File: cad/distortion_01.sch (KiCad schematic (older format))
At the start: 83 parts

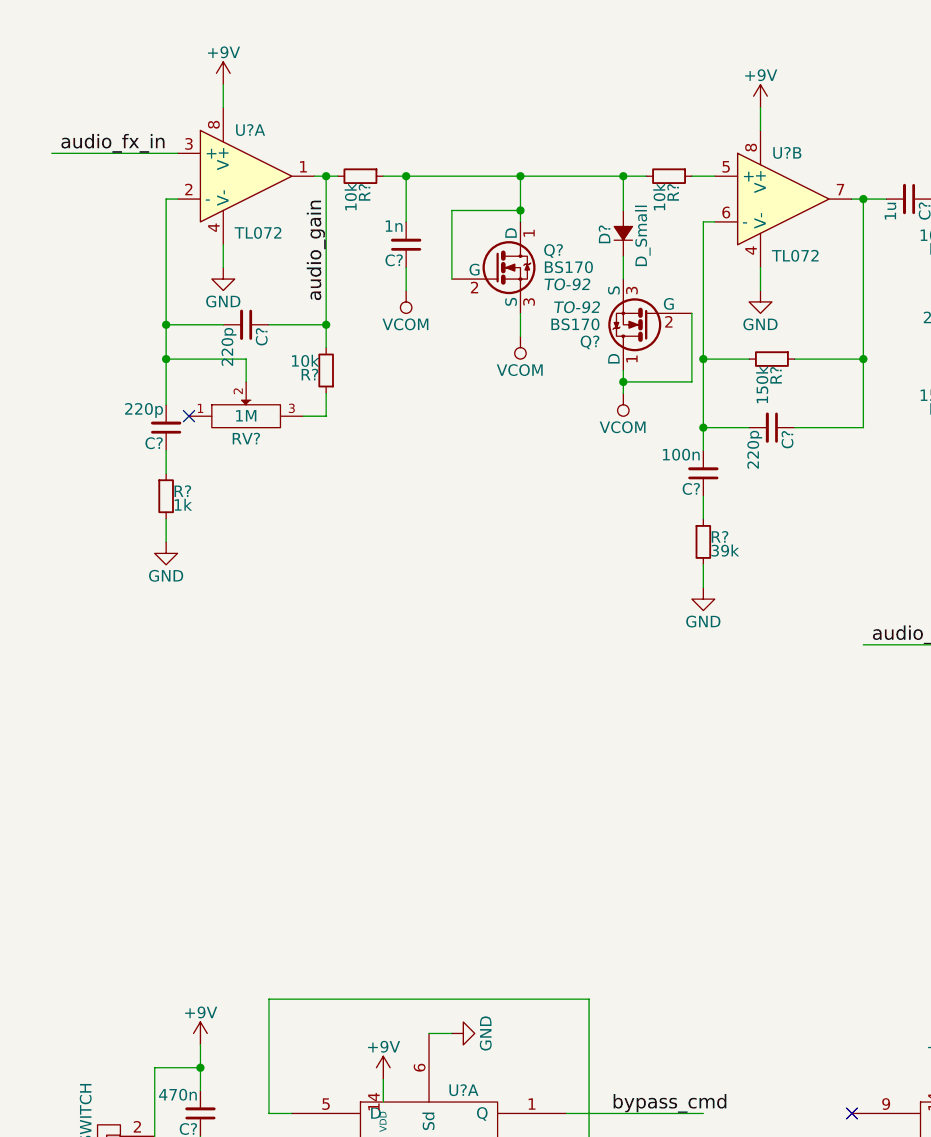
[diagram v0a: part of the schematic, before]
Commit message: Added octave.
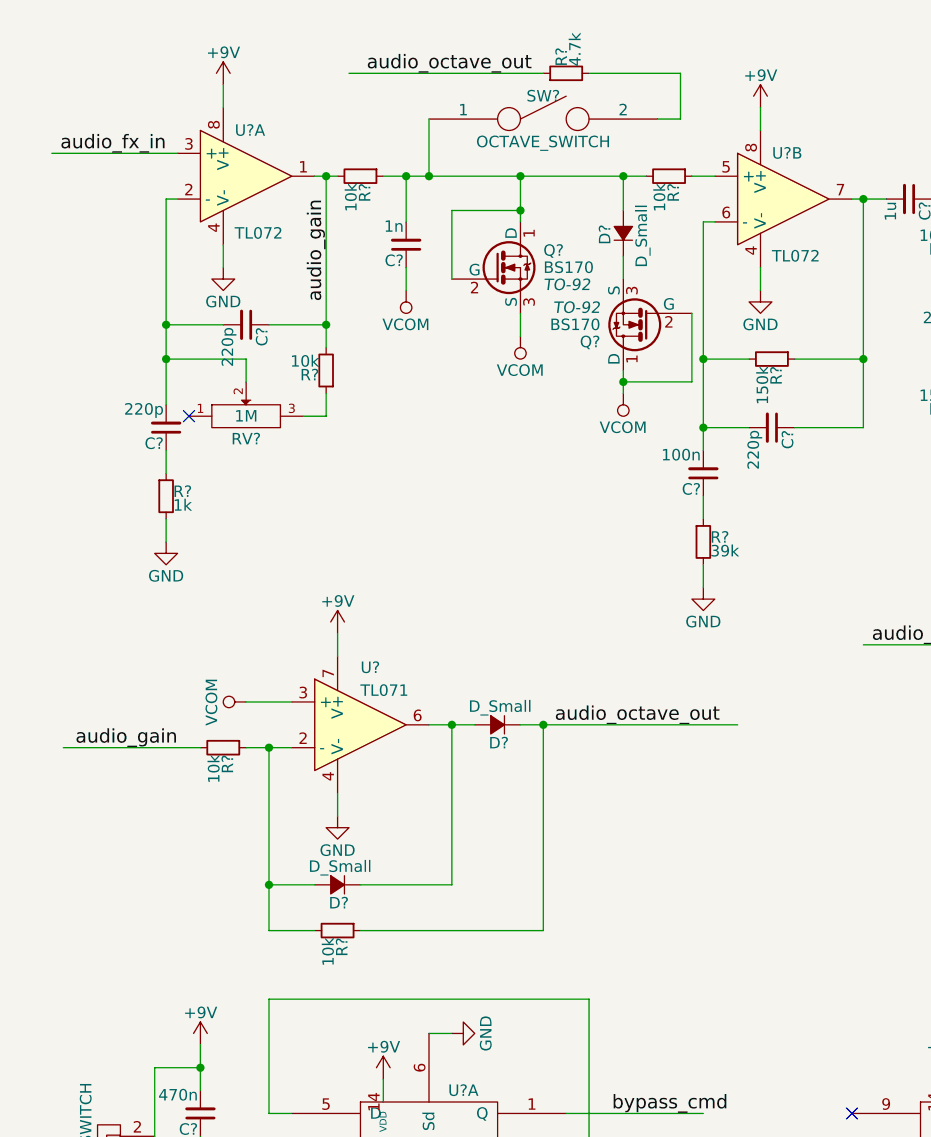
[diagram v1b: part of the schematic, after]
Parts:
- added D? (x2): D_Small, symbol D_Small
- added R? (x2): 10k, symbol R_Small
- added R?: 4.7k, symbol R_Small
- added SW?: OCTAVE_SWITCH, symbol SPST
- added U?: TL071, symbol TL071
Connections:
- net labels added: audio_octave_out
- wire segments 225 -> 244
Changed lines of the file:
@@
 Wire Wire Line
 	4800 3150 4800 3250
+$Comp
+L TL071 U?
+U 1 1 589F853A
+P 2000 3500
+F 0 "U?" H 2000 3750 50  0000 L CNN
+F 1 "TL071" H 2000 3650 50  0000 L CNN
+F 2 "" H 2050 3700 50  0000 C CNN
+F 3 "" H 2000 3750 50  0000 C CNN
+	1    2000 3500
+	1    0    0    -1
+$EndComp
+$Comp
+L +9V #PWR?
+U 1 1 589F8B22
+P 1900 3100
+F 0 "#PWR?" H 1900 2950 50  0001 C CNN
+F 1 "+9V" H 1900 3240 50  0000 C CNN
+F 2 "" H 1900 3100 50  0000 C CNN
+F 3 "" H 1900 3100 50  0000 C CNN
+	1    1900 3100
+	1    0    0    -1
+$EndComp
+$Comp
+L GND #PWR?
+U 1 1 589F8C29
+P 1900 3900
+F 0 "#PWR?" H 1900 3650 50  0001 C CNN
+F 1 "GND" H 1900 3750 50  0000 C CNN
+F 2 "" H 1900 3900 50  0000 C CNN
+F 3 "" H 1900 3900 50  0000 C CNN
+	1    1900 3900
+	1    0    0    -1
+$EndComp
+Wire Wire Line
+	1900 3900 1900 3800
+Wire Wire Line
+	1900 3100 1900 3200
+$Comp
+L D_Small D?
+U 1 1 589F916A
+P 2600 3500
+F 0 "D?" H 2550 3580 50  0000 L CNN
+F 1 "D_Small" H 2450 3420 50  0000 L CNN
+F 2 "" V 2600 3500 50  0000 C CNN
+F 3 "" V 2600 3500 50  0000 C CNN
+	1    2600 3500
+	-1   0    0    1
+$EndComp
+$Comp
+L D_Small D?
+U 1 1 589F92E7
+P 1900 4200
+F 0 "D?" H 1850 4280 50  0000 L CNN
+F 1 "D_Small" H 1750 4120 50  0000 L CNN
+F 2 "" V 1900 4200 50  0000 C CNN
+F 3 "" V 1900 4200 50  0000 C CNN
+	1    1900 4200
+	-1   0    0    1
+$EndComp
+$Comp
+L R_Small R?
+U 1 1 589F9435
+P 1400 3600
+F 0 "R?" H 1430 3620 50  0000 L CNN
+F 1 "10k" H 1430 3560 50  0000 L CNN
+F 2 "" H 1400 3600 50  0000 C CNN
+F 3 "" H 1400 3600 50  0000 C CNN
+	1    1400 3600
+	0    1    1    0
+$EndComp
+Wire Wire Line
+	1500 3600 1700 3600
+Wire Wire Line
+	1800 4200 1600 4200
+Wire Wire Line
+	1600 3600 1600 4400
+Connection ~ 1600 3600
+Wire Wire Line
+	2300 3500 2500 3500
+$Comp
+L R_Small R?
+U 1 1 589F9A7E
+P 1900 4400
+F 0 "R?" H 1930 4420 50  0000 L CNN
+F 1 "10k" H 1930 4360 50  0000 L CNN
+F 2 "" H 1900 4400 50  0000 C CNN
+F 3 "" H 1900 4400 50  0000 C CNN
+	1    1900 4400
+	0    1    1    0
+$EndComp
+Wire Wire Line
+	1600 4400 1800 4400
+Connection ~ 1600 4200
+$Comp
+L R_Small R?
+U 1 1 589F9DEF
+P 2900 650
+F 0 "R?" H 2930 670 50  0000 L CNN
+F 1 "4.7k" H 2930 610 50  0000 L CNN
+F 2 "" H 2900 650 50  0000 C CNN
+F 3 "" H 2900 650 50  0000 C CNN
+	1    2900 650
+	0    -1   -1   0
+$EndComp
+Wire Wire Line
+	2000 4200 2400 4200
+Wire Wire Line
+	2400 4200 2400 3500
+Connection ~ 2400 3500
+Wire Wire Line
+	2000 4400 2800 4400
+Wire Wire Line
+	2800 4400 2800 3500
+Connection ~ 2800 3500
+$Comp
+L VCOM #PWR?
+U 1 1 589FA54D
+P 1500 3400
+F 0 "#PWR?" H 1500 3250 50  0001 C CNN
+F 1 "VCOM" H 1500 3550 50  0000 C CNN
+F 2 "" H 1500 3400 50  0000 C CNN
+F 3 "" H 1500 3400 50  0000 C CNN
+	1    1500 3400
+	0    -1   -1   0
+$EndComp
+Wire Wire Line
+	1500 3400 1700 3400
+Wire Wire Line
+	1300 3600 700  3600
+Text Label 1200 3600 2    60   ~ 0
+audio_gain
+Wire Wire Line
+	2300 850  2300 1100
+Connection ~ 2300 1100
+Text Label 2750 650  2    60   ~ 0
+audio_octave_out
+Wire Wire Line
+	2700 3500 3650 3500
+Text Label 2850 3500 0    60   ~ 0
+audio_octave_out
+$Comp
+L SPST SW?
+U 1 1 589FEE66
+P 2800 850
+F 0 "SW?" H 2800 950 50  0000 C CNN
+F 1 "OCTAVE_SWITCH" H 2800 750 50  0000 C CNN
+F 2 "" H 2800 850 50  0000 C CNN
+F 3 "" H 2800 850 50  0000 C CNN
+	1    2800 850
+	1    0    0    -1
+$EndComp
+Wire Wire Line
+	3000 650  3400 650
+Wire Wire Line
+	3400 650  3400 850
+Wire Wire Line
+	3400 850  3300 850
+Wire Wire Line
+	2800 650  1950 650
 $EndSCHEMATC

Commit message: Simulated OCD / octave part.
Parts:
- removed SW?: OCTAVE_SWITCH, symbol SPST
- removed U?: TL071, symbol TL071
- added D? (x2): D_Small, symbol D_Small
- added R? (x2): 10k, symbol R_Small
- added SW?: OCTAVE_PRE_POST_SWITCH, symbol SWITCH_INV_MSM
- added SW?: HALF-FULLWAVE_SWITCH, symbol SPST
- added U? (x2): TL072, symbol TL072
- C?: value 220p -> 68n
- R?: value 4.7k -> 2.2k
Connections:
- wire segments 244 -> 265
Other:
- moved on the sheet: C?, D?, P?, Q?, R?, RV?, U?A, U?B, U?C, U?D

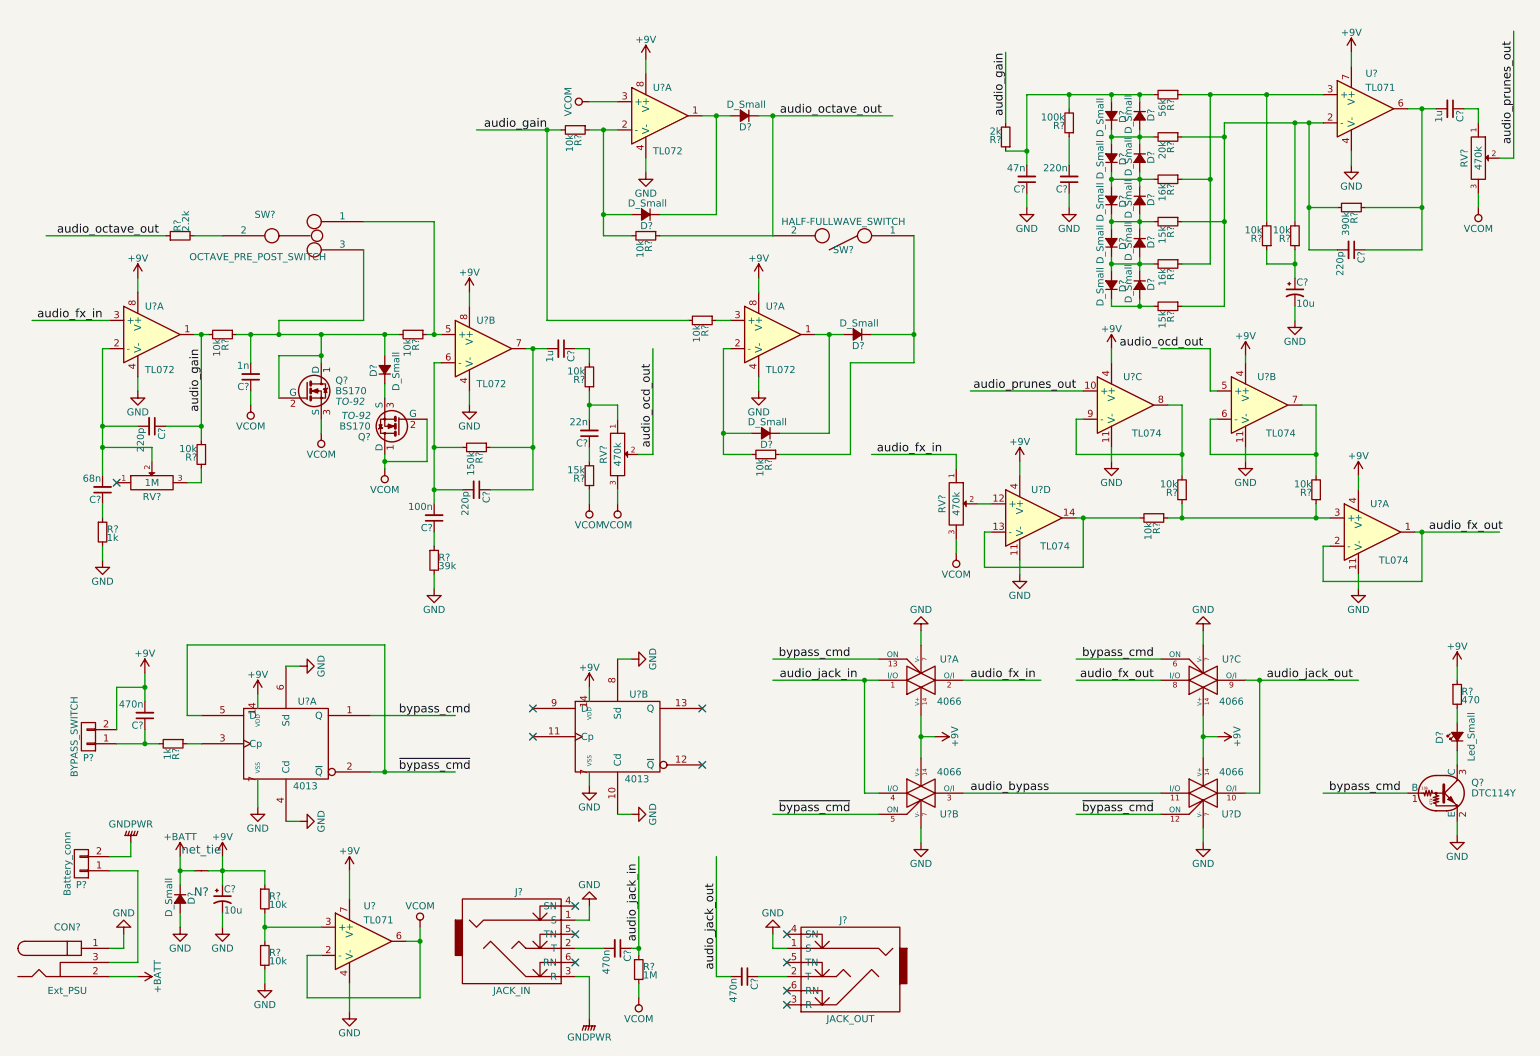
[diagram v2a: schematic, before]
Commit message: Added gain for dry signal. Assigned footprints (TBC).
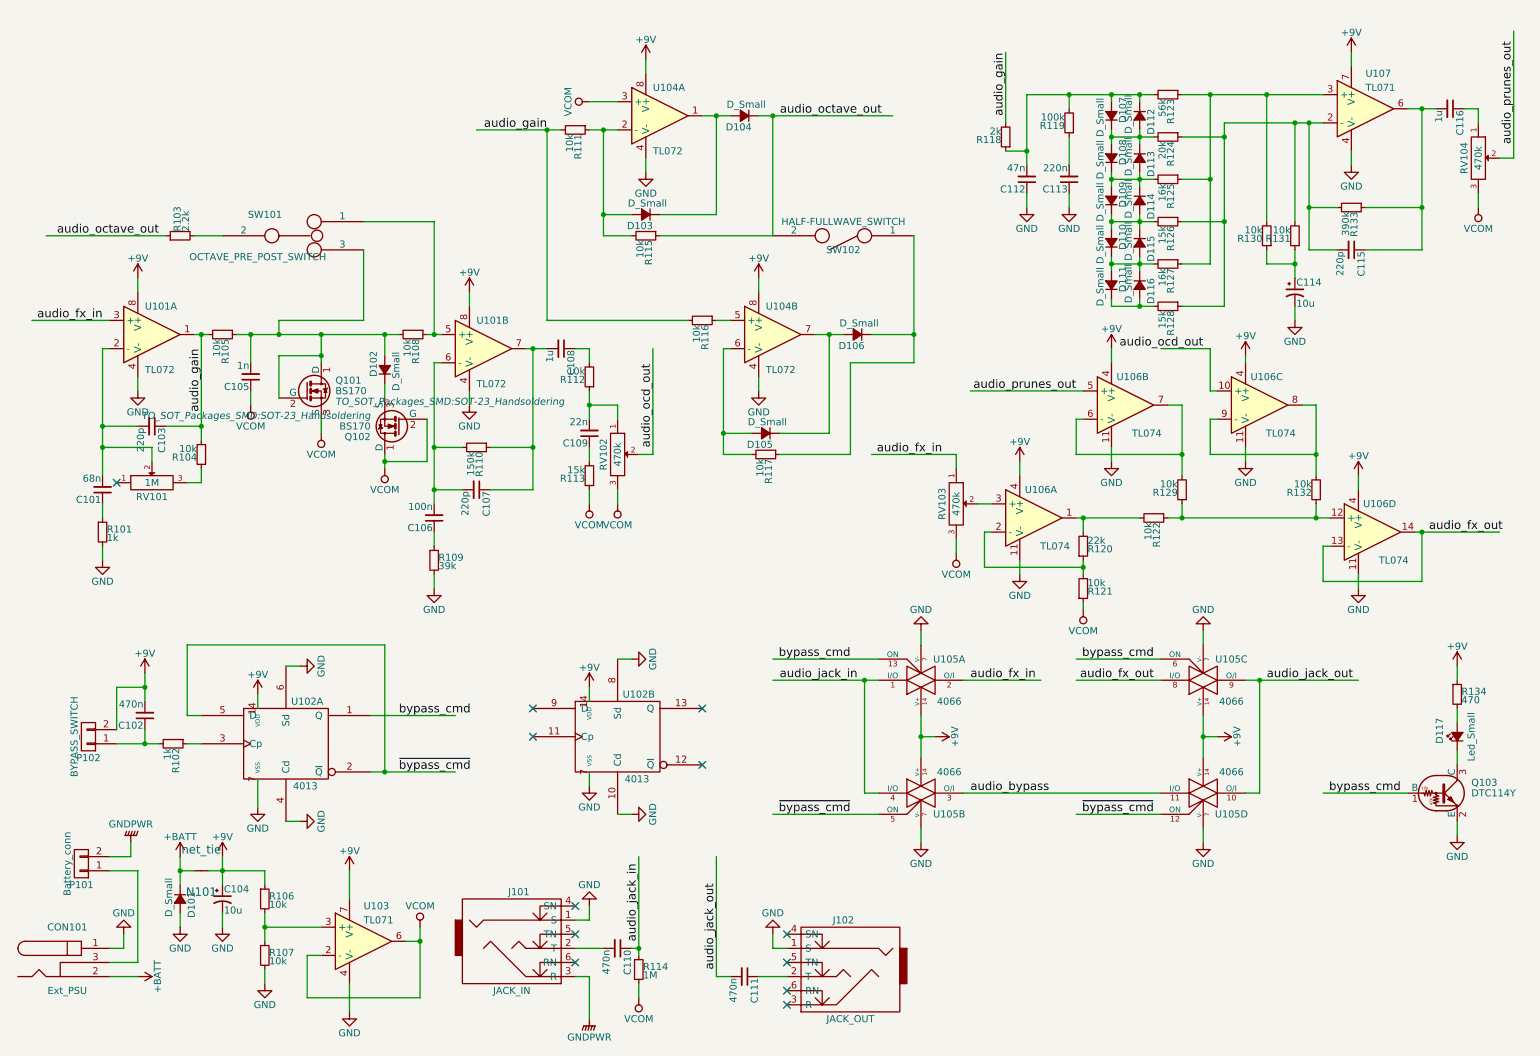
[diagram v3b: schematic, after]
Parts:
- added R120: 22k, Resistors_SMD:R_0603_HandSoldering, symbol R_Small
- added R121: 10k, Resistors_SMD:R_0603_HandSoldering, symbol R_Small
- C101, C103, C105, C106, C107, C109, C112, C113, C115: renamed from C?; footprint (none) -> Capacitors_SMD:C_0603_HandSoldering
- C102, C108, C110, C111, C116: renamed from C?; footprint (none) -> Capacitors_SMD:C_0805_HandSoldering
- C104, C114: renamed from C?; footprint (none) -> Capacitors_SMD:CP_Elec_5x4.5
- CON101: renamed from CON?; footprint (none) -> Connect:JACK_ALIM
- D101: renamed from D?; footprint (none) -> Diodes_SMD:D_SMA_Handsoldering
- D102, D103, D104, D105, D106, D107, D108, D109, D110, D111, D112, D113, D114, D115, D116: renamed from D?; footprint (none) -> TO_SOT_Packages_SMD:SOT-23_Handsoldering
- D117: renamed from D?; footprint (none) -> Pin_Headers:Pin_Header_Straight_1x02_Pitch2.54mm
- J101, J102: renamed from J?; footprint (none) -> Connect:NMJ6HCD2
- N101: renamed from N?; footprint (none) -> flax_lib:net_tie_0.5mm
- P101, P102: renamed from P?; footprint (none) -> Pin_Headers:Pin_Header_Straight_1x02_Pitch2.54mm
- Q101, Q102: renamed from Q?; footprint TO-92 -> TO_SOT_Packages_SMD:SOT-23_Handsoldering
- Q103: renamed from Q?; footprint (none) -> TO_SOT_Packages_SMD:SOT-23_Handsoldering
- R101, R102, R103, R104, R105, R106, R107, R108, R109, R110, R111, R112, R113, R114, R115, R116, R117, R118, R119, R122, R123, R124, R125, R126, R127, R128, R129, R130, R131, R132, R133: renamed from R?; footprint (none) -> Resistors_SMD:R_0603_HandSoldering
- R134: renamed from R?; footprint (none) -> Resistors_SMD:R_0805_HandSoldering
- RV101, RV102, RV103, RV104: renamed from RV?; footprint (none) -> flax_lib:alpha_rv141F
- SW101, SW102: renamed from SW?; footprint (none) -> flax_lib:SW_SPDT_through_hole
- U101, U103, U104, U107: renamed from U?; footprint (none) -> SMD_Packages:SOIC-8-N
- U102, U105, U106: renamed from U?; footprint (none) -> SMD_Packages:SOIC-14_N
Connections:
- wire segments 265 -> 267

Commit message: Added names on pots.
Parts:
- renumbered RV103 to RV_DRY101, RV101 to RV_GAIN101, RV102 to RV_OCD101, RV104 to RV_PRUNES101
